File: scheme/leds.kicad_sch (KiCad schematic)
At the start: 10 parts, among them SW701 RESET, SW702 USER

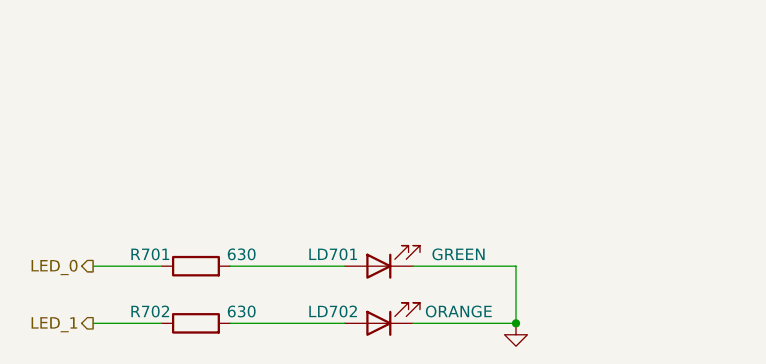
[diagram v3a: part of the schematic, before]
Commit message: feat(schematic): add MPN/LCSC fields and fix Q201 pinout
Подготовка к заказу сборки на JLCPCB:
- всем монтируемым символам добавлено скрытое поле LCSC (коды
  проверены через API JLCPCB, по возможности Basic);
- LSE Y101: Epson FC-135 CL 7 пФ (Q13FC13500002), C106/C108 6.8p C0G,
  footprint под ручную пайку; в SDK нужен LSEDRV=10;
- бусины: FB101/FB401 GZ2012D601TF, FB301 BLM21PG221SN1D (2 А);
- Y401 25 МГц X49SD25MSD2SC (CL 20 пФ), C401/C402 27p -> 33p;
- Y201 8 МГц X49SD8MSD2SC, нагрузочные 22p оставлены (предел F103
  25 пФ, сдвиг частоты для USB FS несущественен);
- C505 100n на ~CARD_DET (антидребезг), ссылка на чертёж Hirose.

Исправления:
- Q201: символ SS9013 с распиновкой TO-92 (1=E 2=B 3=C) стоял на
  footprint SOT-23 (1=B 2=E 3=C) - транзистор встал бы неправильно.
  Заменён на MMBT3904 (SOT-23, Basic), цепи B/E/C сохранены;
- лист leds переведён с 1206 на 0805, R701/R702 630 -> 680 Ом
  (630 нет в E24), LD702 ORANGE -> RED;
- C301 (DNP) получил номинал 4.7n, опечатка 25Mhz в Y401.

ERC: 0 ошибок, 0 предупреждений.
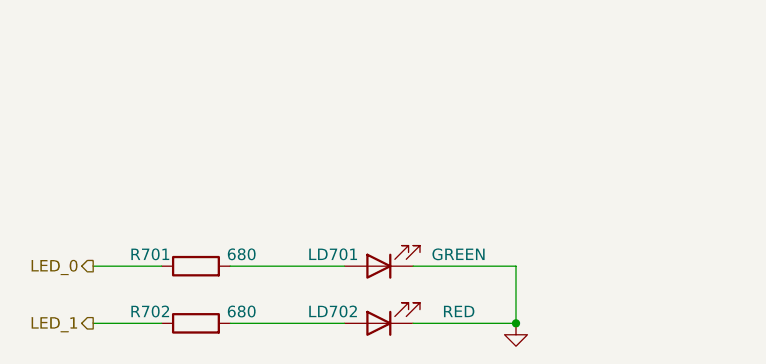
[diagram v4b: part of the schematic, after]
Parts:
- C701, C702: footprint Capacitor_SMD:C_1206_3216Metric_Pad1.33x1.80mm_HandSolder -> Capacitor_SMD:C_0805_2012Metric; LCSC (none) -> C49678
- LD701: footprint LED_SMD:LED_1206_3216Metric_Pad1.42x1.75mm_HandSolder -> LED_SMD:LED_0805_2012Metric; LCSC (none) -> C2297
- LD702: value ORANGE -> RED; footprint LED_SMD:LED_1206_3216Metric_Pad1.42x1.75mm_HandSolder -> LED_SMD:LED_0805_2012Metric; LCSC (none) -> C84256
- R701, R702: value 630 -> 680; footprint Resistor_SMD:R_1206_3216Metric_Pad1.30x1.75mm_HandSolder -> Resistor_SMD:R_0805_2012Metric; LCSC (none) -> C17798
- R703, R704: footprint Resistor_SMD:R_1206_3216Metric_Pad1.30x1.75mm_HandSolder -> Resistor_SMD:R_0805_2012Metric; LCSC (none) -> C149504
- SW701, SW702: LCSC (none) -> C221880
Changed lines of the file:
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@@
 			)
 		)
-		(property "Value" "630"
+		(property "Value" "680"
 			(at 92.71 140.97 90)
 			(show_name no)
@@
 			)
 		)
-		(property "Footprint" "Resistor_SMD:R_1206_3216Metric_Pad1.30x1.75mm_HandSolder"
+		(property "Footprint" "Resistor_SMD:R_0805_2012Metric"
 			(at 87.63 144.018 90)
 			(hide yes)
@@
 		(property "Description" ""
 			(at 87.63 142.24 0)
+			(show_name no)
+			(do_not_autoplace no)
+			(effects
+				(font
+					(size 1.27 1.27)
+				)
+			)
+		)
+		(property "LCSC" "C17798"
+			(at 87.63 142.24 0)
+			(hide yes)
 			(show_name no)
 			(do_not_autoplace no)
@@
 			)
 		)
-		(property "Footprint" "Capacitor_SMD:C_1206_3216Metric_Pad1.33x1.80mm_HandSolder"
+		(property "Footprint" "Capacitor_SMD:C_0805_2012Metric"
 			(at 155.2448 66.04 0)
 			(hide yes)
@@
 		(property "Description" ""
 			(at 156.21 69.85 0)
+			(show_name no)
+			(do_not_autoplace no)
+			(effects
+				(font
+					(size 1.27 1.27)
+				)
+			)
+		)
+		(property "LCSC" "C49678"
+			(at 156.21 69.85 0)
+			(hide yes)
 			(show_name no)
 			(do_not_autoplace no)
@@
 			)
 		)
-		(property "Footprint" "Resistor_SMD:R_1206_3216Metric_Pad1.30x1.75mm_HandSolder"
+		(property "Footprint" "Resistor_SMD:R_0805_2012Metric"
 			(at 103.632 53.34 90)
 			(hide yes)
@@
 		(property "Description" ""
 			(at 105.41 53.34 0)
+			(show_name no)
+			(do_not_autoplace no)
+			(effects
+				(font
+					(size 1.27 1.27)
+				)
+			)
+		)
+		(property "LCSC" "C149504"
+			(at 105.41 53.34 0)
+			(hide yes)
 			(show_name no)
 			(do_not_autoplace no)
@@
 			)
 		)
-		(property "Footprint" "Resistor_SMD:R_1206_3216Metric_Pad1.30x1.75mm_HandSolder"
+		(property "Footprint" "Resistor_SMD:R_0805_2012Metric"
 			(at 172.212 54.61 90)
 			(hide yes)
@@
 		(property "Description" ""
 			(at 173.99 54.61 0)
+			(show_name no)
+			(do_not_autoplace no)
+			(effects
+				(font
+					(size 1.27 1.27)
+				)
+			)
+		)
+		(property "LCSC" "C149504"
+			(at 173.99 54.61 0)
+			(hide yes)
 			(show_name no)
 			(do_not_autoplace no)
@@
 			)
 		)
-		(property "Footprint" "Capacitor_SMD:C_1206_3216Metric_Pad1.33x1.80mm_HandSolder"
+		(property "Footprint" "Capacitor_SMD:C_0805_2012Metric"
 			(at 86.6648 64.77 0)
 			(hide yes)
@@
 		(property "Description" ""
 			(at 87.63 68.58 0)
+			(show_name no)
+			(do_not_autoplace no)
+			(effects
+				(font
+					(size 1.27 1.27)
+				)
+			)
+		)
+		(property "LCSC" "C49678"
+			(at 87.63 68.58 0)
+			(hide yes)
 			(show_name no)
 			(do_not_autoplace no)
@@
 			)
 		)
-		(property "Footprint" "LED_SMD:LED_1206_3216Metric_Pad1.42x1.75mm_HandSolder"
+		(property "Footprint" "LED_SMD:LED_0805_2012Metric"
 			(at 107.95 142.24 0)
 			(hide yes)
@@
 		(property "Description" ""
 			(at 107.95 142.24 0)
+			(show_name no)
+			(do_not_autoplace no)
+			(effects
+				(font
+					(size 1.27 1.27)
+				)
+			)
+		)
+		(property "LCSC" "C2297"
+			(at 107.95 142.24 0)
+			(hide yes)
 			(show_name no)
 			(do_not_autoplace no)
@@
 			)
 		)
-		(property "Value" "ORANGE"
+		(property "Value" "RED"
 			(at 116.84 147.32 0)
 			(show_name no)
@@
 			)
 		)
-		(property "Footprint" "LED_SMD:LED_1206_3216Metric_Pad1.42x1.75mm_HandSolder"
+		(property "Footprint" "LED_SMD:LED_0805_2012Metric"
 			(at 107.95 148.59 0)
 			(hide yes)
@@
 		(property "Description" ""
 			(at 107.95 148.59 0)
+			(show_name no)
+			(do_not_autoplace no)
+			(effects
+				(font
+					(size 1.27 1.27)
+				)
+			)
+		)
+		(property "LCSC" "C84256"
+			(at 107.95 148.59 0)
+			(hide yes)
 			(show_name no)
 			(do_not_autoplace no)
@@
 			)
 		)
+		(property "LCSC" "C221880"
+			(at 105.41 68.58 0)
+			(hide yes)
+			(show_name no)
+			(do_not_autoplace no)
+			(effects
+				(font
+					(size 1.27 1.27)
+				)
+			)
+		)
 		(pin "1"
 		)
@@
 			)
 		)
+		(property "LCSC" "C221880"
+			(at 173.99 69.85 0)
+			(hide yes)
+			(show_name no)
+			(do_not_autoplace no)
+			(effects
+				(font
+					(size 1.27 1.27)
+				)
+			)
+		)
 		(pin "1"
 		)
@@
 			)
 		)
-		(property "Value" "630"
+		(property "Value" "680"
 			(at 92.71 147.32 90)
 			(show_name no)
@@
 			)
 		)
-		(property "Footprint" "Resistor_SMD:R_1206_3216Metric_Pad1.30x1.75mm_HandSolder"
+		(property "Footprint" "Resistor_SMD:R_0805_2012Metric"
 			(at 87.63 150.368 90)
 			(hide yes)
@@
 			(show_name no)
 			(do_not_autoplace no)
+			(effects
+				(font
+					(size 1.27 1.27)
+				)
+			)
+		)
+		(property "LCSC" "C17798"
+			(at 87.63 148.59 0)
+			(hide yes)
+			(show_name no)
+			(do_not_autoplace no)

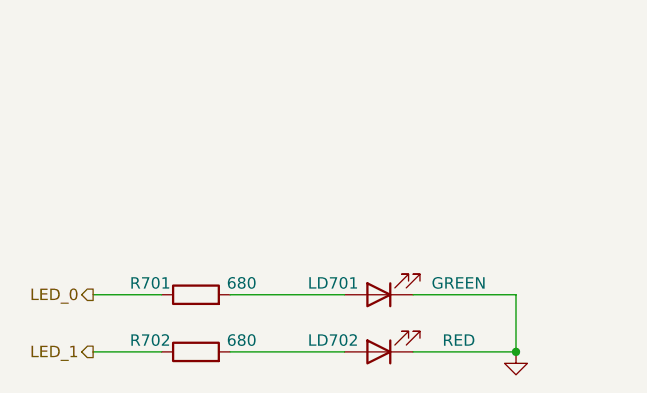
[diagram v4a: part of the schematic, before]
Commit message: feat(pcb): prepare board for placement
- Зелёные LED остаются C2297 (InGaN), резисторы к ним 330 Ом (C17630):
  ток 0.6-2.1 мА при Vf 2.6-3.1 В. Жёлто-зелёные отклонены: по
  даташитам световая отдача на мА у них в ~10 раз ниже.
- Цепи дифпар переименованы, чтобы KiCad распознавал пары:
  J201_D+/-, STL_D+/-, FT_D+/-, RXI_P/N; шаблоны классов USB90/MDI100
  обновлены.
- Отверстия шилда H801-H804: footprint из шаблона Arduino (NPTH 3.2,
  courtyard 3.4) в проектной библиотеке g0_dev_board.pretty вместо M3
  с courtyard 6.9, конфликтовавшего с разъёмами Uno.
- Исправлена арифметика в комментарии к двухцветному LED ST-Link.
- Плата синхронизирована со схемой: паритет 0, нарушений DRC 0.
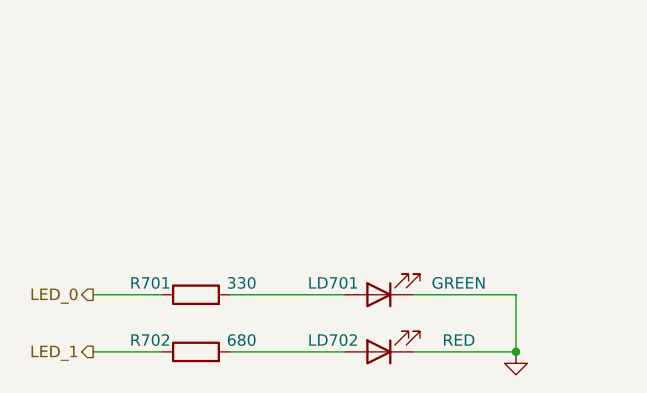
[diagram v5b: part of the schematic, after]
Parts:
- R701: value 680 -> 330; LCSC C17798 -> C17630
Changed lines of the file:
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@@
 			)
 		)
-		(property "Value" "680"
+		(property "Value" "330"
 			(at 92.71 140.97 90)
 			(show_name no)
@@
 			)
 		)
-		(property "LCSC" "C17798"
+		(property "LCSC" "C17630"
 			(at 87.63 142.24 0)
 			(hide yes)
